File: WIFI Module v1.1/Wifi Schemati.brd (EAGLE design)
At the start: 90.1 x 63.4 mm, 25 parts, among them IC1 PIC24FVXXKA302-SP

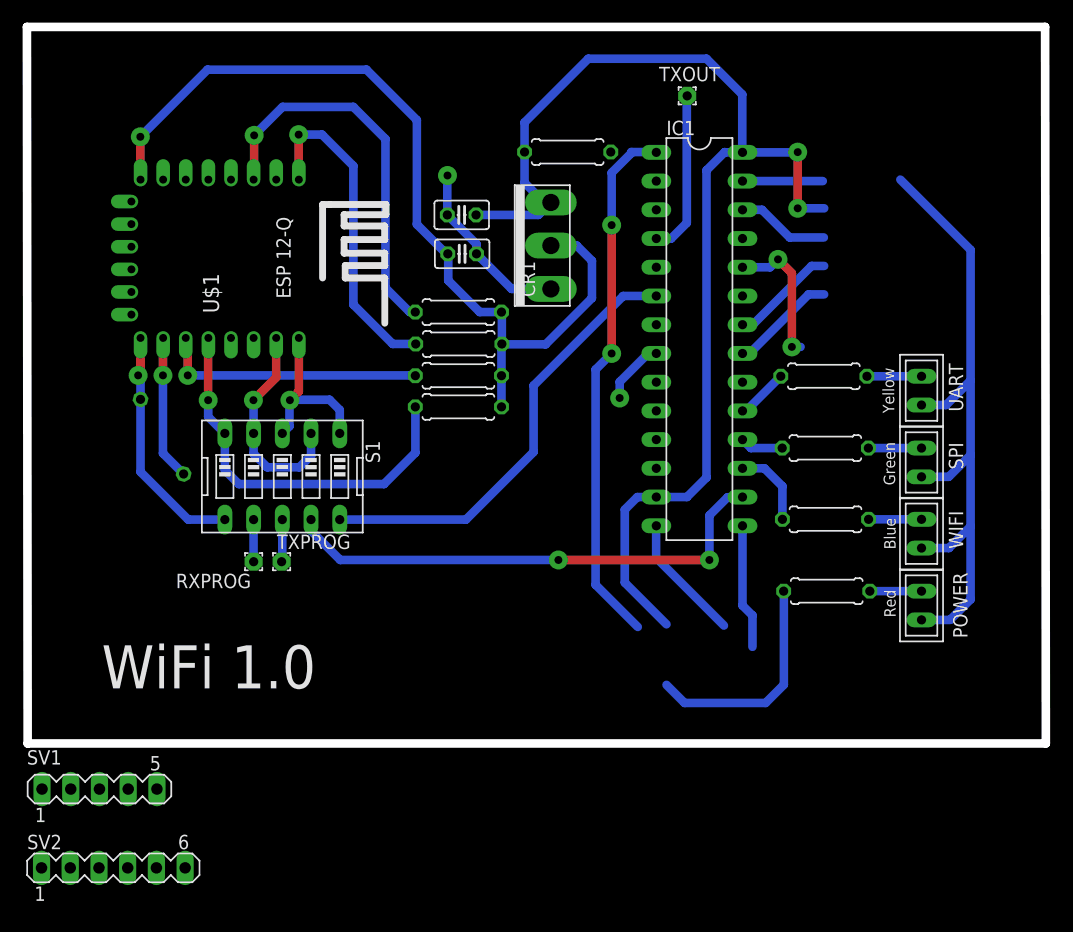
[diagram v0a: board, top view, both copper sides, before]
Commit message: v1.1 SCH and PCB update
Changed SCH and PCB stuff for headers and 3.3v reg
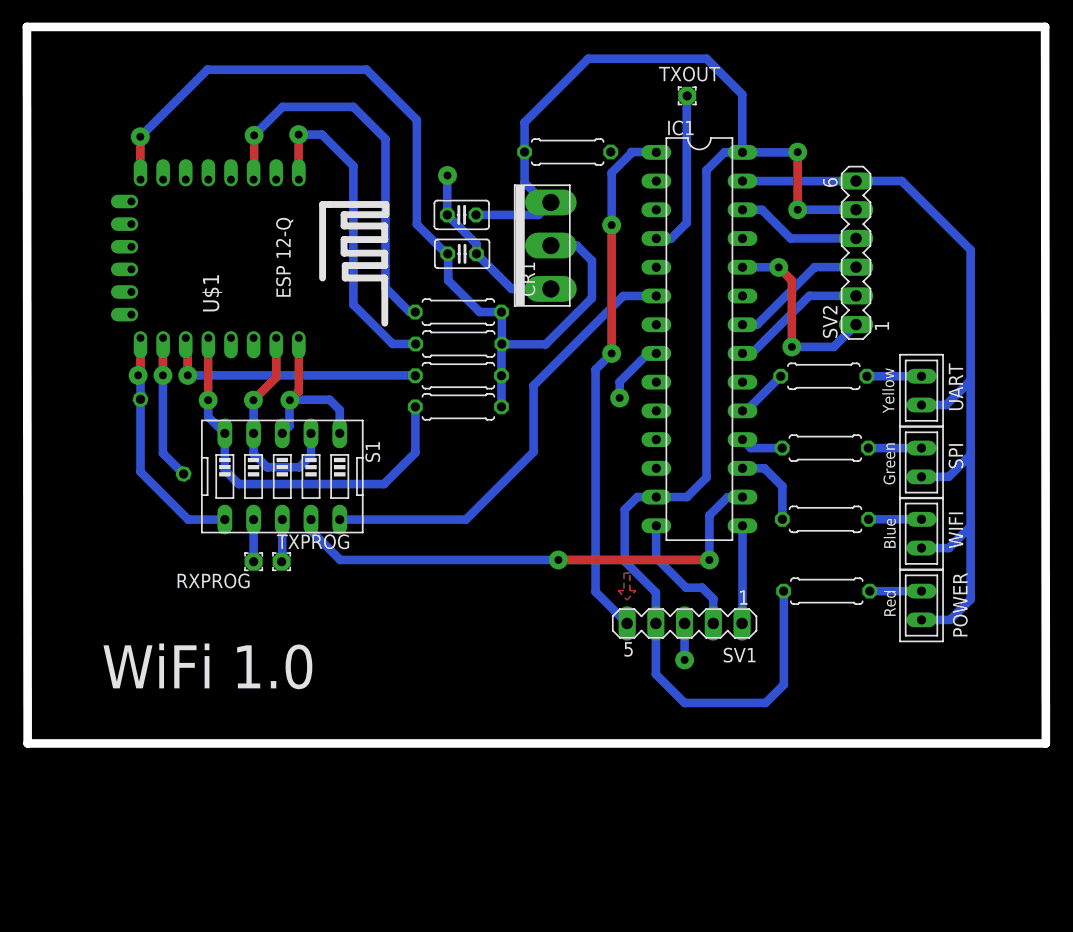
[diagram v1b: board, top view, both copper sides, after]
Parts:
- moved SV2 85.3 mm to (66.9, 7.55), turned to 90 degrees
- moved SV1 53.8 mm to (51.7, -25.2), turned to 180 degrees
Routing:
- net GND: track 110.2 -> 120.2 mm, vias 3 -> 4
- net VDD: track 126.8 -> 135.1 mm
- net MISO: track 12.4 -> 17.2 mm
- net MOSI: track 9.38 -> 12.8 mm
- net SS: track 8.21 -> 11.1 mm
- net CLK: track 9.37 -> 12.2 mm
- net PGC: track 11.1 -> 8.65 mm
- net MCLR: track 47.1 -> 46.4 mm
- added copper zone on layer 1, net N$9
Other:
- board text added: "GND"
